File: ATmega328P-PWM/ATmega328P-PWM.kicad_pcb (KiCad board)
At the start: 2 copper layers, 80 x 59.9 mm, 28 parts, among them IC1 ATMEGA328P-M, P1 AVR_ISP, P2 FTDI_HDR, P3 BAT, P4 PHOTODIODE, P5 SPK, Q1 IRLML6401, Q2 MMBT3906, SW1 PEC12R-2217F, U1 AT25DF041B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

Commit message: Change encoder to PEC09.
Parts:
- added D1: D, Diodes_SMD:SOD-123, F.Cu at (161.0, 104.3)
- added Q3: IRLML6401, TO_SOT_Packages_SMD:SOT-23_Handsoldering, F.Cu at (199.2, 85.9)
- added R10: 0, Resistors_SMD:R_0603_HandSoldering, F.Cu at (167.1, 101.9)
- added R11: 0, Resistors_SMD:R_0603_HandSoldering, F.Cu at (134.6, 102.0)
- added R12: 100k, Resistors_SMD:R_0603_HandSoldering, F.Cu at (176.6, 97.1)
- SW1: value PEC12R-2217F -> PEC092320FS0015; footprint Footprints:PEC12R-2217F -> Footprints:PEC092320FS0015
- moved SW1 9.65 mm to (118.1, 80.4)
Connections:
- P3 pad 1: VCC -> Net-(P3-Pad1)

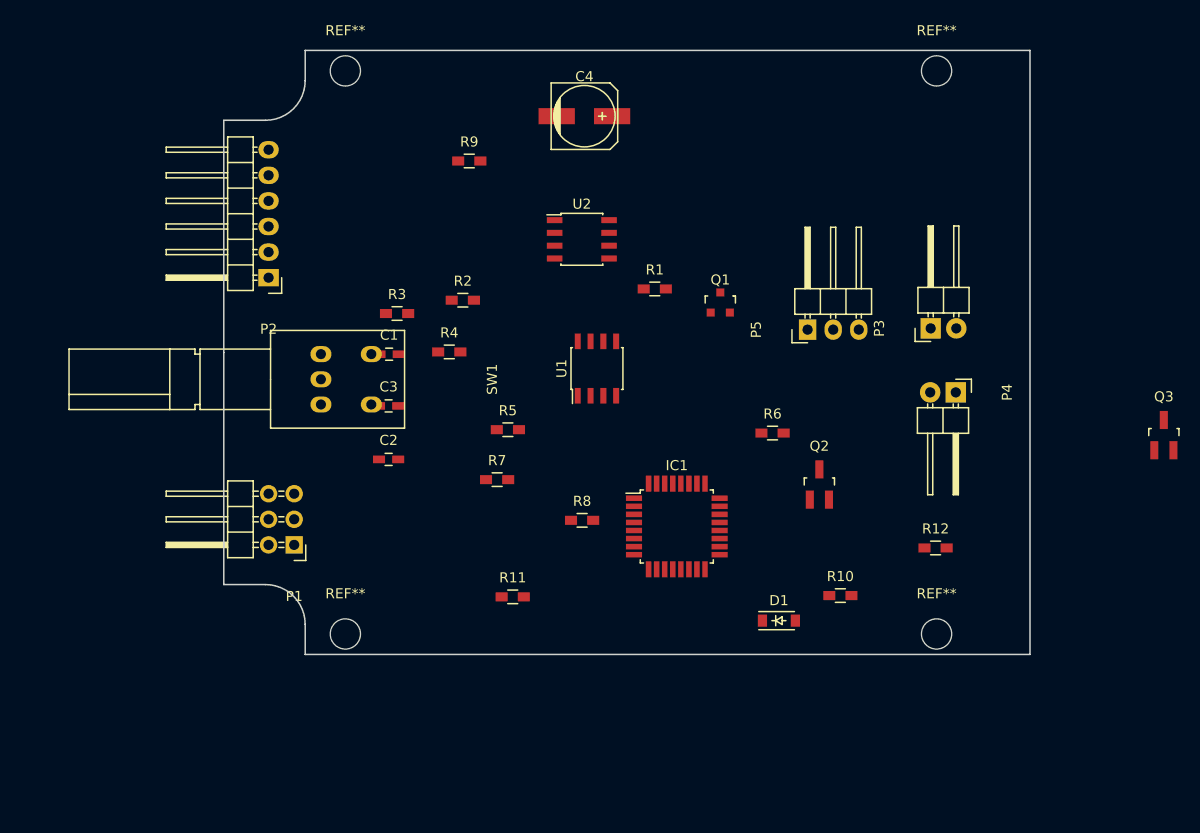
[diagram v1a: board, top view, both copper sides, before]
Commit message: Add bypassing and associate footprints.
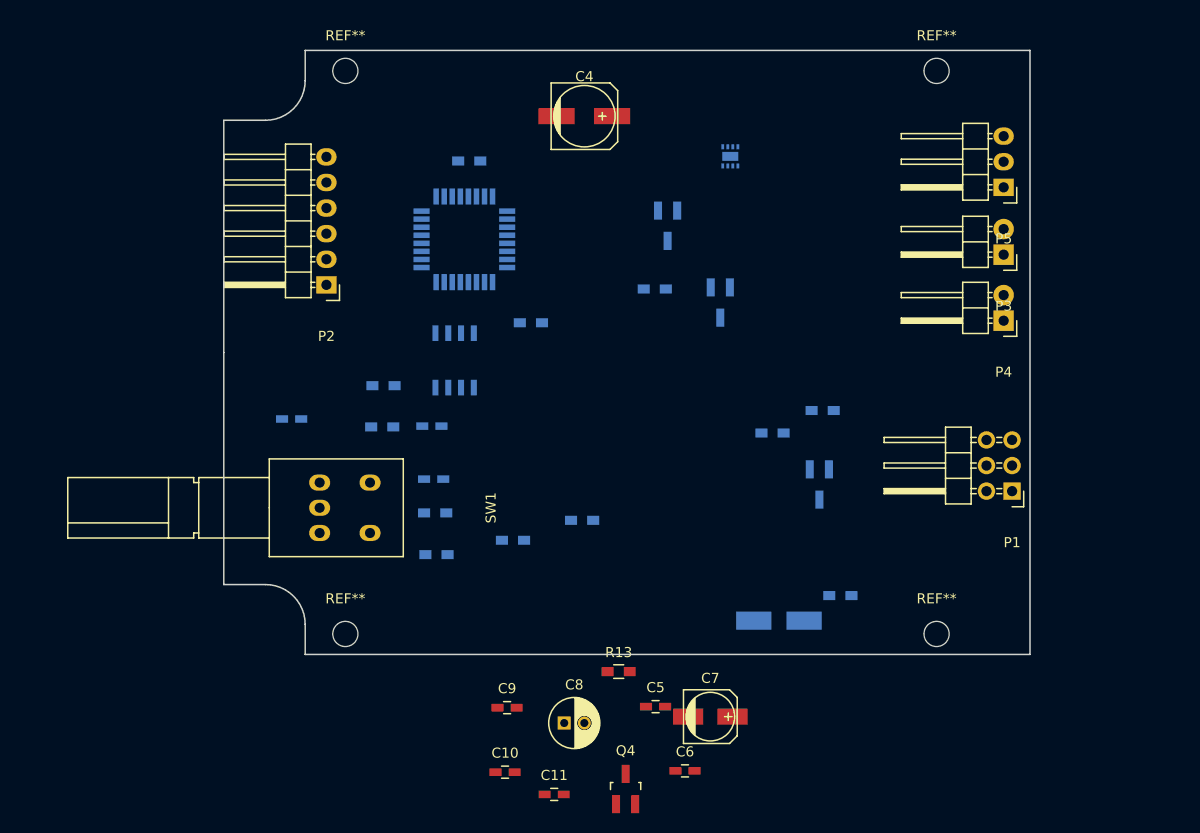
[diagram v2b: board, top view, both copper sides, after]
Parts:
- removed the REF** at (176.7, 105.7)
- removed the REF** at (176.7, 49.8)
- removed the REF** at (118.0, 49.8)
- removed the REF** at (118.0, 105.7)
- added C10: 100n, Capacitors_SMD:C_0603_HandSoldering, F.Cu at (133.8, 119.4)
- added C11: 100n, Capacitors_SMD:C_0603_HandSoldering, F.Cu at (138.7, 121.6)
- added C5: 100n, Capacitors_SMD:C_0603_HandSoldering, F.Cu at (148.8, 112.9)
- added C6: 100n, Capacitors_SMD:C_0603_HandSoldering, F.Cu at (151.7, 119.3)
- added C7: 47u, Capacitors_SMD:c_elec_5x5.3, F.Cu at (154.2, 113.9)
- added C8: 47u, Capacitors_ThroughHole:C_Radial_D5_L11_P2, F.Cu at (139.7, 114.5)
- added C9: 100n, Capacitors_SMD:C_0603_HandSoldering, F.Cu at (134.0, 113.0)
- added Q4: MMBT3906, TO_SOT_Packages_SMD:SOT-23_Handsoldering, F.Cu at (145.8, 121.1)
- added R13: 1k, Resistors_SMD:R_0603_HandSoldering, F.Cu at (145.1, 109.4)
- added REF**: MountingHole_2-5mm, Mounting_Holes:MountingHole_2-5mm, F.Cu at (176.7, 49.8)
- added REF**: MountingHole_2-5mm, Mounting_Holes:MountingHole_2-5mm, F.Cu at (118.0, 49.8)
- added REF**: MountingHole_2-5mm, Mounting_Holes:MountingHole_2-5mm, F.Cu at (118.0, 105.7)
- added REF**: MountingHole_2-5mm, Mounting_Holes:MountingHole_2-5mm, F.Cu at (176.7, 105.7)
- C1, C2, C3, IC1, Q3, R1, R10, R11, R12, R2, R3, R4, R5, R6, R7, R8, R9, U1: moved to B.Cu
- D1: footprint Diodes_SMD:SOD-123 -> Diodes_SMD:SMA_Handsoldering; moved to B.Cu
- Q1: footprint Housings_SOT-23_SOT-143_TSOT-6:SOT-23 -> TO_SOT_Packages_SMD:SOT-23_Handsoldering; moved to B.Cu
- Q2: footprint Housings_SOT-23_SOT-143_TSOT-6:SOT-23_Handsoldering -> TO_SOT_Packages_SMD:SOT-23_Handsoldering; moved to B.Cu
- U2: footprint Housings_SOIC:SOIC-8_3.9x4.9mm_Pitch1.27mm -> Footprints:S-PWSON-N8; moved to B.Cu
- moved P1 71.4 mm to (184.2, 91.5)
- moved Q3 53.5 mm to (150.0, 65.2)
- moved IC1 35.4 mm to (129.8, 66.5)
- moved P5 24.0 mm to (183.3, 61.3), turned to 180 degrees
- moved R12 17.6 mm to (165.4, 83.5)
- moved U2 16.9 mm to (156.2, 58.3)
- moved U1 14.1 mm to (128.8, 78.5), turned to 270 degrees
- moved SW1 12.8 mm to (117.9, 93.1)
- moved R3 11.3 mm to (121.6, 85.1)
- moved R5 11.0 mm to (126.9, 93.6)
- moved P3 10.3 mm to (183.3, 68.0), turned to 180 degrees
- moved C3 9.71 mm to (112.6, 84.3)
- moved R7 9.57 mm to (127.0, 97.8)
- moved P4 8.55 mm to (183.3, 74.6), turned to 180 degrees
- moved C1 8.30 mm to (126.6, 85.0)
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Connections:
- IC1 pad 10: Net-(IC1-Pad10) -> /ENC_HI
- IC1 pad 11: Net-(IC1-Pad11) -> //VAUX_ON
- IC1 pad 12: Net-(IC1-Pad12) -> /ENC_BUT
- IC1 pad 13: Net-(IC1-Pad13) -> /PWM_1
- IC1 pad 14: Net-(IC1-Pad14) -> /PWM_2
- IC1 pad 18: Net-(IC1-Pad18) -> VCC
- IC1 pad 2: Net-(IC1-Pad2) -> //FLASH_CS
- IC1 pad 25: Net-(IC1-Pad25) -> /ENC_A
- IC1 pad 26: Net-(IC1-Pad26) -> /ENC_B
- IC1 pad 32: Net-(IC1-Pad32) -> /PHOTOD

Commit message: Layout, but poorly.
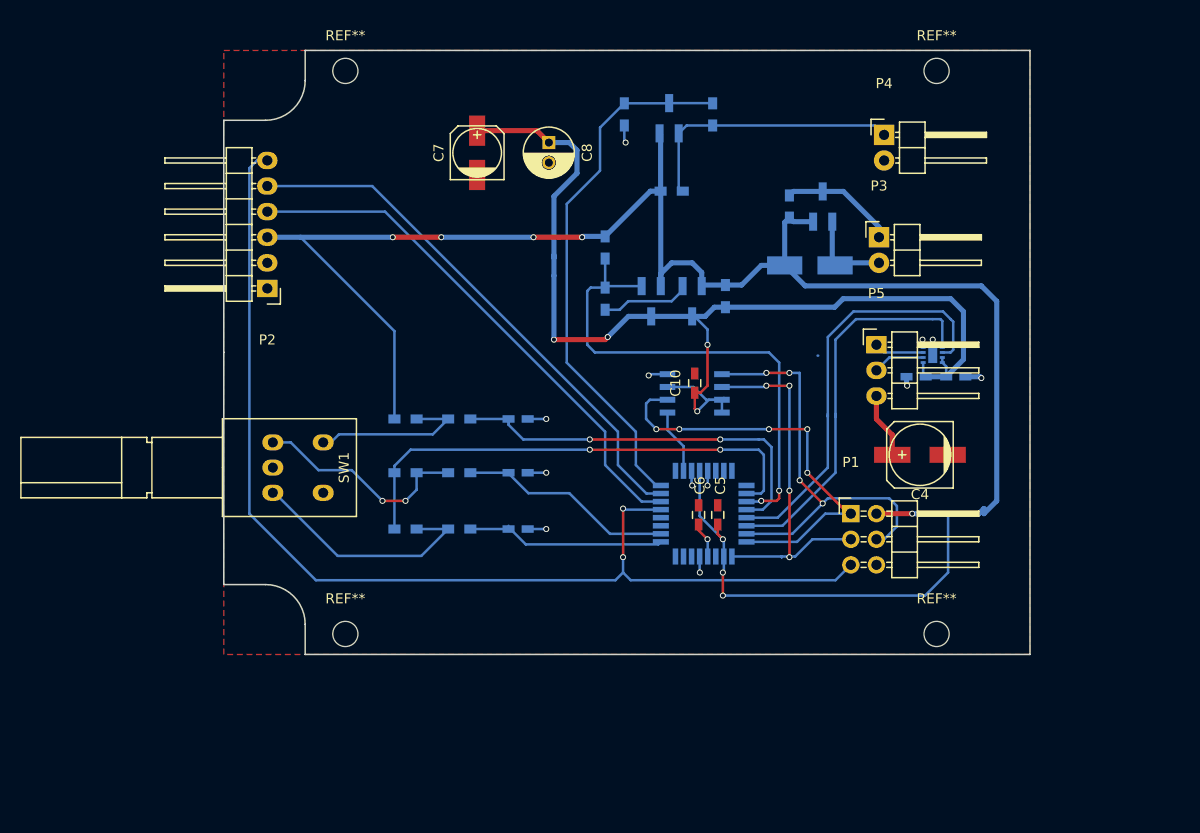
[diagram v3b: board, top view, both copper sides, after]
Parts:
- C11, C9, Q4, R13: moved to B.Cu
- moved C7 60.6 mm to (131.1, 57.9), turned to 90 degrees
- moved C8 57.6 mm to (138.2, 56.9), turned to 270 degrees
- moved C11 57.5 mm to (178.6, 80.1)
- moved C9 52.2 mm to (174.6, 80.1), turned to 180 degrees
- moved R10 49.4 mm to (154.4, 54.1), turned to 270 degrees
- moved Q4 48.9 mm to (152.4, 72.6)
- moved C4 47.3 mm to (175.0, 87.9), turned to 180 degrees
- moved R11 43.0 mm to (162.1, 63.2), turned to 90 degrees
- moved C10 43.0 mm to (152.7, 80.8), turned to 90 degrees
- moved Q2 39.3 mm to (150.1, 54.5), turned to 180 degrees
- moved R13 37.0 mm to (143.8, 72.4), turned to 90 degrees
- moved R6 36.6 mm to (124.0, 89.7)
- moved IC1 36.1 mm to (153.5, 93.7), turned to 270 degrees
- moved D1 35.4 mm to (164.1, 69.1), turned to 180 degrees
- moved U2 28.1 mm to (176.3, 78.0), turned to 90 degrees
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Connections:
- C2 pad 1: Net-(C2-Pad1) -> /ENC_A
- C8 pad 1: Net-(C8-Pad1) -> /VAUX
- IC1 pad 30: Net-(IC1-Pad30) -> /RX
- IC1 pad 31: Net-(IC1-Pad31) -> /TX
- P1 pad 5: /RESET -> //RESET
- P2 pad 6: /RST -> //RESET
- P5 pad 2: /SPK2 -> /SPK1
- Q2 pad 2: Net-(Q2-Pad2) -> VCC
- R12 pad 1: Net-(Q2-Pad2) -> VCC
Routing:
- net VCC: track 0.00 -> 201.8 mm, vias 0 -> 8
- net //RESET: track 0.00 -> 110.2 mm, vias 0 -> 2
- net /VAUX: track 0.00 -> 108.3 mm, vias 0 -> 4
- net /TX: track 0.00 -> 53.6 mm
- net /PHOTOD: track 0.00 -> 53.2 mm
- net /RX: track 0.00 -> 52.9 mm
- net //VAUX_ON: track 0.00 -> 50.4 mm, vias 0 -> 2
- net /ENC_HI: track 0.00 -> 49.2 mm, vias 0 -> 2
- net /MOSI: track 0.00 -> 43.0 mm, vias 0 -> 4
- net /MISO: track 0.00 -> 42.1 mm, vias 0 -> 5
- net /PWM_1: track 0.00 -> 41.2 mm
- net /ENC_BUT: track 0.00 -> 39.9 mm, vias 0 -> 2
- net /PWM_2: track 0.00 -> 38.6 mm
- net /SCK: track 0.00 -> 36.7 mm, vias 0 -> 4
- net GND: track 0.00 -> 27.5 mm, vias 0 -> 12
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- added copper zone on F.Cu, net GND
